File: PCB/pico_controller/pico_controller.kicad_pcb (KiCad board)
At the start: 2 copper layers, 54 x 40.5 mm, 22 parts, among them J1 Conn_01x04, J10 Conn_01x03, J11 Conn_01x03, J2 Conn_01x04, J3 Conn_01x04, J4 Conn_01x12, J5 Conn_01x04, J6 Conn_01x02, J7 Conn_01x02, J8 Conn_01x04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

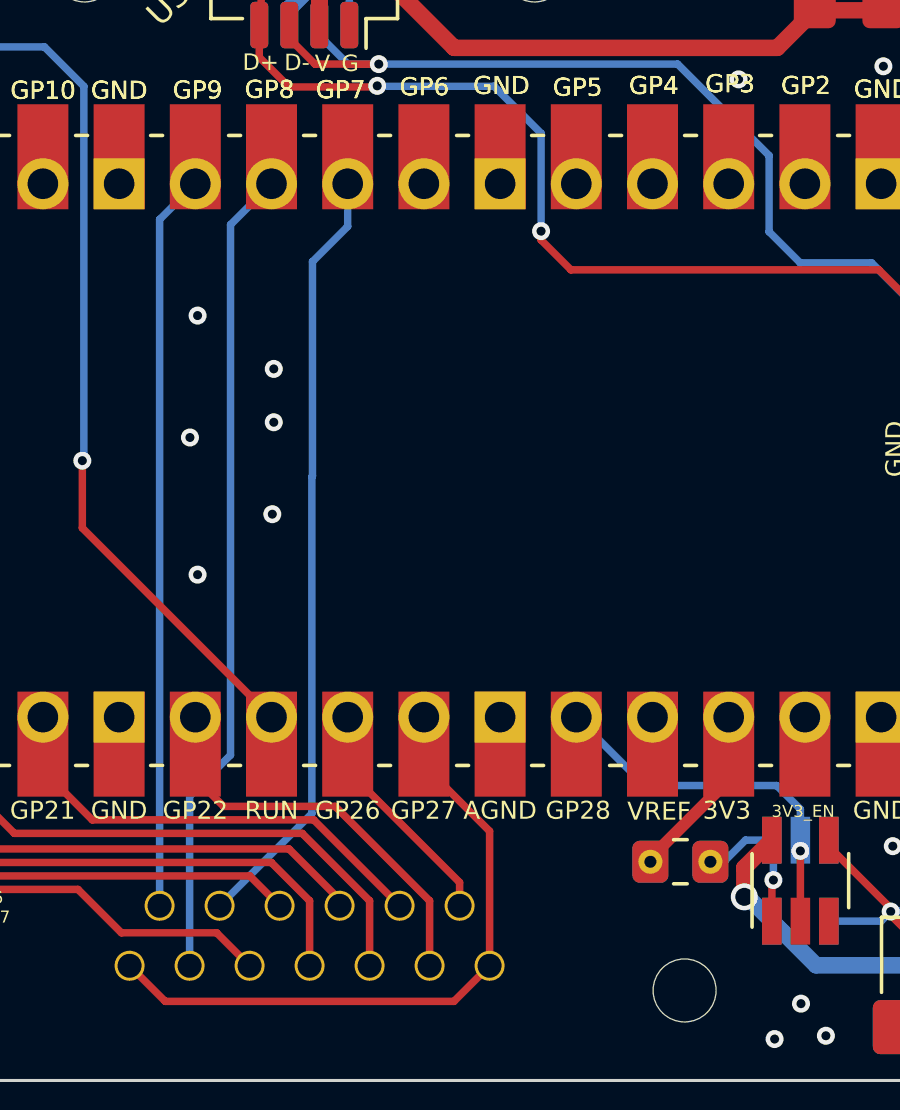
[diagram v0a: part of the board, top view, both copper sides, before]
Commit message: add handness jumper to controller
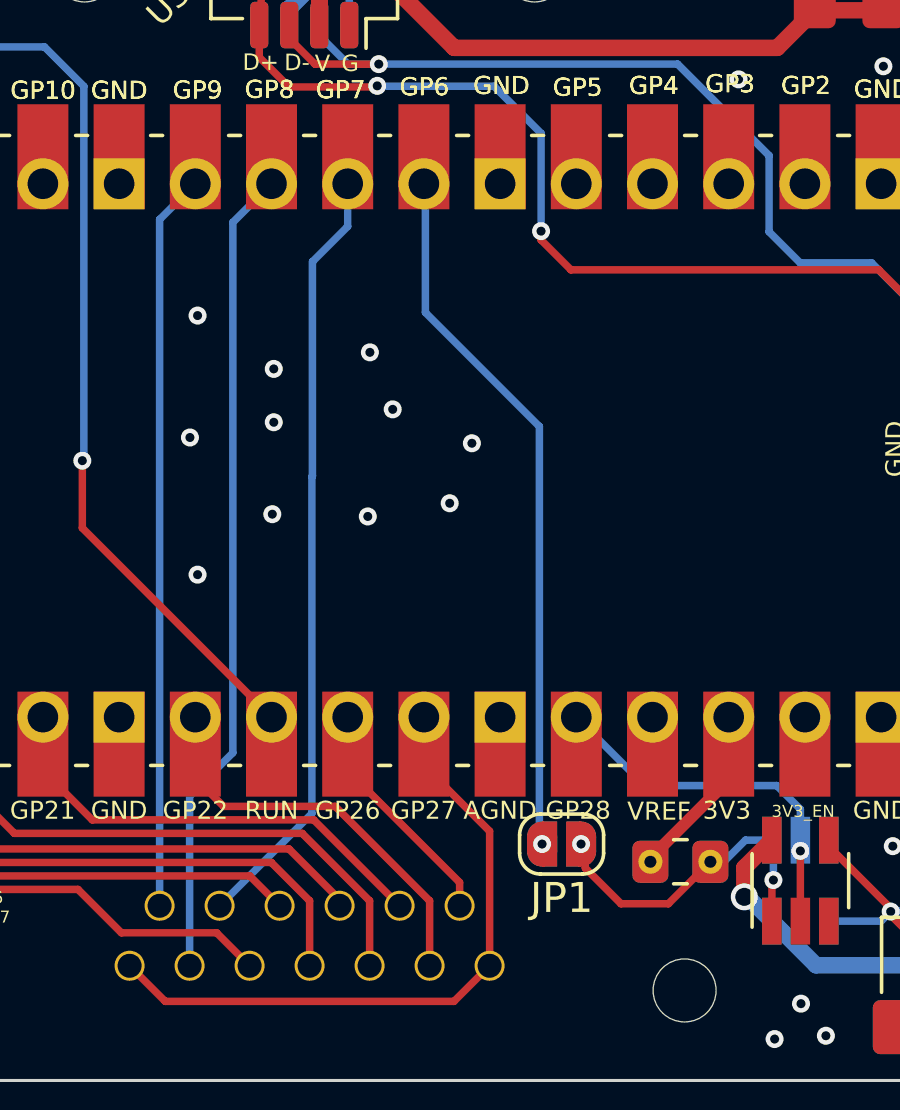
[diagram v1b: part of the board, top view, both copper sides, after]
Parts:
- added JP1: Jumper_2_Bridged, Jumper:SolderJumper-2_P1.3mm_Open_RoundedPad1.0x1.5mm, F.Cu at (108.4, 113.1)
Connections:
- U1 pad 9: unconnected-(U1-Pad9) -> Handness
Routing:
- net Handness: track 0.00 -> 23.6 mm, vias 0 -> 1
- net OE: track 5.09 -> 11.2 mm, vias 1 -> 2
- net GND: vias 23 -> 28

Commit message: without led
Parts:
- H1, H2, H3, H4: footprint MountingHole:MountingHole_2.1mm -> ergodash_controller:MountingHole_2.1mm
- J1, J2, J3, J5, J8, J9: footprint Connector_JST:JST_SH_SM04B-SRSS-TB_1x04-1MP_P1.00mm_Horizontal -> ergodash_controller:JST_SH_SM04B-SRSS-TB_1x04-1MP_P1.00mm_Horizontal
- J10, J11: footprint Connector_JST:JST_SH_SM03B-SRSS-TB_1x03-1MP_P1.00mm_Horizontal -> ergodash_controller:JST_SH_SM03B-SRSS-TB_1x03-1MP_P1.00mm_Horizontal
- J6, J7: footprint Connector_JST:JST_SHL_SM02B-SHLS-TF_1x02-1MP_P1.00mm_Horizontal -> ergodash_controller:JST_SHL_SM02B-SHLS-TF_1x02-1MP_P1.00mm_Horizontal
- JP1: footprint Jumper:SolderJumper-2_P1.3mm_Open_RoundedPad1.0x1.5mm -> ergodash_controller:SolderJumper-2_P1.3mm_Open_RoundedPad1.0x1.5mm
- R1, R2: footprint Resistor_SMD:R_0805_2012Metric_Pad1.20x1.40mm_HandSolder -> ergodash_controller:R_0805_2012Metric_Pad1.20x1.40mm_HandSolder
- SW1: footprint Button_Switch_THT:SW_PUSH_6mm -> ergodash_controller:SW_PUSH_6mm
- U2, U3: footprint Package_TO_SOT_SMD:SOT-23-5_HandSoldering -> ergodash_controller:SOT-23-5_HandSoldering
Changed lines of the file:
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@@
   (net 39 "OE")
   (net 40 "Handness")
-  (footprint "Connector_JST:JST_SH_SM04B-SRSS-TB_1x04-1MP_P1.00mm_Horizontal" (layer "F.Cu")
+  (footprint "ergodash_controller:JST_SH_SM04B-SRSS-TB_1x04-1MP_P1.00mm_Horizontal" (layer "F.Cu")
     (at 123.64 84.05 90)
     (descr "JST SH series connector, SM04B-SRSS-TB (http://www.jst-mfg.com/product/pdf/eng/eSH.pdf), generated with kicad-footprint-generator")
@@
     )
   )
-  (footprint "Resistor_SMD:R_0805_2012Metric_Pad1.20x1.40mm_HandSolder" (layer "F.Cu")
+  (footprint "ergodash_controller:R_0805_2012Metric_Pad1.20x1.40mm_HandSolder" (layer "F.Cu")
     (at 116.84 84.328 90)
     (descr "Resistor SMD 0805 (2012 Metric), square (rectangular) end terminal, IPC_7351 nominal with elongated pad for handsoldering. (Body size source: IPC-SM-782 page 72, https://www.pcb-3d.com/wordpress/wp-content/uploads/ipc-sm-782a_amendment_1_and_2.pdf), generated with kicad-footprint-generator")
@@
     )
   )
-  (footprint "Connector_JST:JST_SHL_SM02B-SHLS-TF_1x02-1MP_P1.00mm_Horizontal" (layer "F.Cu")
+  (footprint "ergodash_controller:JST_SHL_SM02B-SHLS-TF_1x02-1MP_P1.00mm_Horizontal" (layer "F.Cu")
     (at 77 84 180)
     (descr "JST SHL series connector, SM02B-SHLS-TF (http://www.jst-mfg.com/product/pdf/eng/eSHL.pdf), generated with kicad-footprint-generator")
@@
     )
   )
-  (footprint "MountingHole:MountingHole_2.1mm" (layer "F.Cu")
+  (footprint "ergodash_controller:MountingHole_2.1mm" (layer "F.Cu")
     (at 92.5 84)
     (descr "Mounting Hole 2.1mm, no annular")
@@
     (pad "" np_thru_hole circle (at 0 0) (size 2.1 2.1) (drill 2.1) (layers *.Cu *.Mask))
   )
-  (footprint "MountingHole:MountingHole_2.1mm" (layer "F.Cu")
+  (footprint "ergodash_controller:MountingHole_2.1mm" (layer "F.Cu")
     (at 107.5 84)
     (descr "Mounting Hole 2.1mm, no annular")
@@
     (pad "" np_thru_hole circle (at 0 0) (size 2.1 2.1) (drill 2.1) (layers *.Cu *.Mask))
   )
-  (footprint "Resistor_SMD:R_0805_2012Metric_Pad1.20x1.40mm_HandSolder" (layer "F.Cu")
+  (footprint "ergodash_controller:R_0805_2012Metric_Pad1.20x1.40mm_HandSolder" (layer "F.Cu")
     (at 119.126 84.328 90)
     (descr "Resistor SMD 0805 (2012 Metric), square (rectangular) end terminal, IPC_7351 nominal with elongated pad for handsoldering. (Body size source: IPC-SM-782 page 72, https://www.pcb-3d.com/wordpress/wp-content/uploads/ipc-sm-782a_amendment_1_and_2.pdf), generated with kicad-footprint-generator")
@@
     )
   )
-  (footprint "MountingHole:MountingHole_2.1mm" (layer "F.Cu")
+  (footprint "ergodash_controller:MountingHole_2.1mm" (layer "F.Cu")
     (at 87.5 118)
     (descr "Mounting Hole 2.1mm, no annular")
@@
     (pad "" np_thru_hole circle (at 0 0) (size 2.1 2.1) (drill 2.1) (layers *.Cu *.Mask))
   )
-  (footprint "Connector_JST:JST_SH_SM03B-SRSS-TB_1x03-1MP_P1.00mm_Horizontal" (layer "F.Cu")
+  (footprint "ergodash_controller:JST_SH_SM03B-SRSS-TB_1x03-1MP_P1.00mm_Horizontal" (layer "F.Cu")
     (at 76.83 116.82 -90)
     (descr "JST SH series connector, SM03B-SRSS-TB (http://www.jst-mfg.com/product/pdf/eng/eSH.pdf), generated with kicad-footprint-generator")
@@
     )
   )
-  (footprint "Button_Switch_THT:SW_PUSH_6mm" (layer "F.Cu")
+  (footprint "ergodash_controller:SW_PUSH_6mm" (layer "F.Cu")
     (at 88 86.5 180)
     (descr "https://www.omron.com/ecb/products/pdf/en-b3f.pdf")
@@
     )
   )
-  (footprint "MountingHole:MountingHole_2.1mm" (layer "F.Cu")
+  (footprint "ergodash_controller:MountingHole_2.1mm" (layer "F.Cu")
     (at 112.5 118)
     (descr "Mounting Hole 2.1mm, no annular")
@@
     (pad "" np_thru_hole circle (at 0 0) (size 2.1 2.1) (drill 2.1) (layers *.Cu *.Mask))
   )
-  (footprint "Connector_JST:JST_SH_SM04B-SRSS-TB_1x04-1MP_P1.00mm_Horizontal" (layer "F.Cu")
+  (footprint "ergodash_controller:JST_SH_SM04B-SRSS-TB_1x04-1MP_P1.00mm_Horizontal" (layer "F.Cu")
     (at 122.174 117.348)
     (descr "JST SH series connector, SM04B-SRSS-TB (http://www.jst-mfg.com/product/pdf/eng/eSH.pdf), generated with kicad-footprint-generator")
@@
     )
   )
-  (footprint "Jumper:SolderJumper-2_P1.3mm_Open_RoundedPad1.0x1.5mm" (layer "F.Cu")
+  (footprint "ergodash_controller:SolderJumper-2_P1.3mm_Open_RoundedPad1.0x1.5mm" (layer "F.Cu")
     (at 108.4 113.12 180)
     (descr "SMD Solder Jumper, 1x1.5mm, rounded Pads, 0.3mm gap, open")
@@
       (options (clearance outline) (anchor rect))
       (primitives
-        (gr_circle (center 0 0.25) (end -0.5 0.25) (width 0) (fill yes))
-        (gr_circle (center 0 -0.25) (end -0.5 -0.25) (width 0) (fill yes))
+        (gr_circle (center 0 0.25) (end 0.5 0.25) (width 0) (fill yes))
+        (gr_circle (center 0 -0.25) (end 0.5 -0.25) (width 0) (fill yes))
         (gr_poly (pts
             (xy -0.5 0.75)
@@
       (options (clearance outline) (anchor rect))
       (primitives
-        (gr_circle (center 0 0.25) (end -0.5 0.25) (width 0) (fill yes))
-        (gr_circle (center 0 -0.25) (end -0.5 -0.25) (width 0) (fill yes))
+        (gr_circle (center 0 0.25) (end 0.5 0.25) (width 0) (fill yes))
+        (gr_circle (center 0 -0.25) (end 0.5 -0.25) (width 0) (fill yes))
         (gr_poly (pts
             (xy 0 0.75)
@@
       ))
   )
-  (footprint "Connector_JST:JST_SH_SM04B-SRSS-TB_1x04-1MP_P1.00mm_Horizontal" (layer "F.Cu")
+  (footprint "ergodash_controller:JST_SH_SM04B-SRSS-TB_1x04-1MP_P1.00mm_Horizontal" (layer "F.Cu")
     (at 99.822 83.82 180)
     (descr "JST SH series connector, SM04B-SRSS-TB (http://www.jst-mfg.com/product/pdf/eng/eSH.pdf), generated with kicad-footprint-generator")
@@
     )
   )
-  (footprint "Package_TO_SOT_SMD:SOT-23-5_HandSoldering" (layer "F.Cu")
+  (footprint "ergodash_controller:SOT-23-5_HandSoldering" (layer "F.Cu")
     (at 116.36 114.34 90)
     (descr "5-pin SOT23 package")
@@
     )
   )
-  (footprint "Connector_JST:JST_SH_SM04B-SRSS-TB_1x04-1MP_P1.00mm_Horizontal" (layer "B.Cu")
+  (footprint "ergodash_controller:JST_SH_SM04B-SRSS-TB_1x04-1MP_P1.00mm_Horizontal" (layer "B.Cu")
     (at 123.64 84.05 -90)
     (descr "JST SH series connector, SM04B-SRSS-TB (http://www.jst-mfg.com/product/pdf/eng/eSH.pdf), generated with kicad-footprint-generator")
@@
     )
   )
-  (footprint "Connector_JST:JST_SHL_SM02B-SHLS-TF_1x02-1MP_P1.00mm_Horizontal" (layer "B.Cu")
+  (footprint "ergodash_controller:JST_SHL_SM02B-SHLS-TF_1x02-1MP_P1.00mm_Horizontal" (layer "B.Cu")
     (at 77 84)
     (descr "JST SHL series connector, SM02B-SHLS-TF (http://www.jst-mfg.com/product/pdf/eng/eSHL.pdf), generated with kicad-footprint-generator")
@@
     )
   )
-  (footprint "Connector_JST:JST_SH_SM03B-SRSS-TB_1x03-1MP_P1.00mm_Horizontal" (layer "B.Cu")
+  (footprint "ergodash_controller:JST_SH_SM03B-SRSS-TB_1x03-1MP_P1.00mm_Horizontal" (layer "B.Cu")
     (at 76.83 116.82 90)
     (descr "JST SH series connector, SM03B-SRSS-TB (http://www.jst-mfg.com/product/pdf/eng/eSH.pdf), generated with kicad-footprint-generator")
@@
     )
   )
-  (footprint "Connector_JST:JST_SH_SM04B-SRSS-TB_1x04-1MP_P1.00mm_Horizontal" (layer "B.Cu")
+  (footprint "ergodash_controller:JST_SH_SM04B-SRSS-TB_1x04-1MP_P1.00mm_Horizontal" (layer "B.Cu")
     (at 99.822 83.82)
     (descr "JST SH series connector, SM04B-SRSS-TB (http://www.jst-mfg.com/product/pdf/eng/eSH.pdf), generated with kicad-footprint-generator")
@@
     )
   )
-  (footprint "Package_TO_SOT_SMD:SOT-23-5_HandSoldering" (layer "B.Cu")
+  (footprint "ergodash_controller:SOT-23-5_HandSoldering" (layer "B.Cu")
     (at 116.36 114.34 -90)
     (descr "5-pin SOT23 package")
@@
     )
   )
-  (footprint "Connector_JST:JST_SH_SM04B-SRSS-TB_1x04-1MP_P1.00mm_Horizontal" (layer "B.Cu")
+  (footprint "ergodash_controller:JST_SH_SM04B-SRSS-TB_1x04-1MP_P1.00mm_Horizontal" (layer "B.Cu")
     (at 122.174 117.348 180)
     (descr "JST SH series connector, SM04B-SRSS-TB (http://www.jst-mfg.com/product/pdf/eng/eSH.pdf), generated with kicad-footprint-generator")
